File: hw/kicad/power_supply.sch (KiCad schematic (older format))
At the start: 30 parts, among them U10 LM22675-5.0, U8 LM22675-5.0, U9 AZ1117CR-3.3

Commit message: Changed footprint of and placed bulk cap
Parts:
- C52: footprint Capacitors_ThroughHole:C_Radial_D18_L36_P7.5 -> Capacitors_angled:C_Radial_D18_L37_P7.5_Angled
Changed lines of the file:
@@
 F 0 "C52" H 2275 2150 50  0000 L CNN
 F 1 "2200u/63V1" H 2275 1950 50  0000 L CNN
-F 2 "Capacitors_ThroughHole:C_Radial_D18_L36_P7.5" H 2288 1900 30  0001 C CNN
+F 2 "Capacitors_angled:C_Radial_D18_L37_P7.5_Angled" H 2288 1900 30  0001 C CNN
 F 3 "" H 2250 2050 60  0000 C CNN
 	1    2250 2050

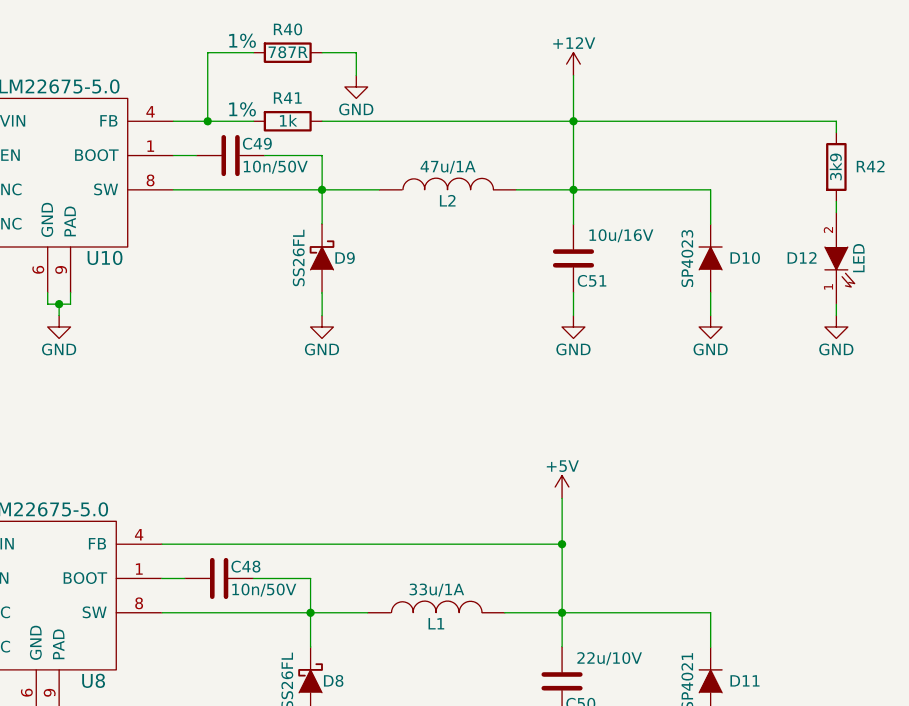
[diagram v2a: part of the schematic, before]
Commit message: Add test pads
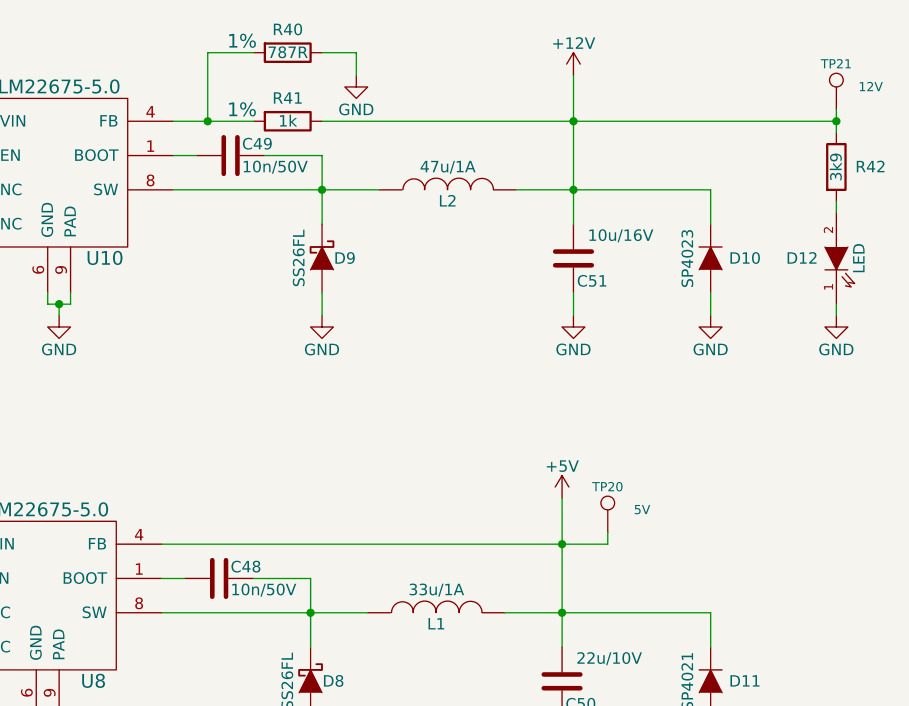
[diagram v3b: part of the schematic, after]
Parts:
- added TP20: 5V, Measurement_Points:Measurement_Point_Round-SMD-Pad_Small, symbol TESTPAD
- added TP21: 12V, Measurement_Points:Measurement_Point_Round-SMD-Pad_Small, symbol TESTPAD
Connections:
- net +12V: now also TP21.1
- net +5V: now also TP20.1
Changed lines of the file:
@@
 $EndDescr
 $Comp
-L +5V #PWR85
+L +5V #PWR077
 U 1 1 582A637E
 P 4500 5200
-F 0 "#PWR85" H 4500 5050 50  0001 C CNN
+F 0 "#PWR077" H 4500 5050 50  0001 C CNN
 F 1 "+5V" H 4500 5340 50  0000 C CNN
 F 2 "" H 4500 5200 60  0000 C CNN
@@
 $EndComp
 $Comp
-L +3.3V #PWR90
+L +3.3V #PWR078
 U 1 1 582A6384
 P 6050 5200
-F 0 "#PWR90" H 6050 5050 50  0001 C CNN
+F 0 "#PWR078" H 6050 5050 50  0001 C CNN
 F 1 "+3.3V" H 6050 5340 50  0000 C CNN
 F 2 "" H 6050 5200 60  0000 C CNN
@@
 Connection ~ 6050 5500
 $Comp
-L GND #PWR88
+L GND #PWR079
 U 1 1 582A63B6
 P 5400 6100
-F 0 "#PWR88" H 5400 5850 50  0001 C CNN
+F 0 "#PWR079" H 5400 5850 50  0001 C CNN
 F 1 "GND" H 5400 5950 50  0000 C CNN
 F 2 "" H 5400 6100 60  0000 C CNN
@@
 $EndComp
 $Comp
-L VPP #PWR77
+L VPP #PWR080
 U 1 1 582A6B17
 P 2250 1550
-F 0 "#PWR77" H 2250 1400 50  0001 C CNN
+F 0 "#PWR080" H 2250 1400 50  0001 C CNN
 F 1 "VPP" H 2250 1700 50  0000 C CNN
 F 2 "" H 2250 1550 60  0000 C CNN
@@
 $EndComp
 $Comp
-L GND #PWR78
+L GND #PWR081
 U 1 1 582A75C3
 P 2250 2600
-F 0 "#PWR78" H 2250 2350 50  0001 C CNN
+F 0 "#PWR081" H 2250 2350 50  0001 C CNN
 F 1 "GND" H 2250 2450 50  0000 C CNN
 F 2 "" H 2250 2600 60  0000 C CNN
@@
 	2250 1550 2250 1900
 $Comp
-L GND #PWR89
+L GND #PWR082
 U 1 1 5830BFE7
 P 5450 2600
-F 0 "#PWR89" H 5450 2350 50  0001 C CNN
+F 0 "#PWR082" H 5450 2350 50  0001 C CNN
 F 1 "GND" H 5450 2450 50  0000 C CNN
 F 2 "" H 5450 2600 60  0000 C CNN
@@
 	7700 1550 7700 2200
 $Comp
-L GND #PWR92
+L GND #PWR083
 U 1 1 5830D1D1
 P 6600 2600
-F 0 "#PWR92" H 6600 2350 50  0001 C CNN
+F 0 "#PWR083" H 6600 2350 50  0001 C CNN
 F 1 "GND" H 6600 2450 50  0000 C CNN
 F 2 "" H 6600 2600 60  0000 C CNN
@@
 	6600 2600 6600 2500
 $Comp
-L GND #PWR97
+L GND #PWR084
 U 1 1 5830D22E
 P 7700 2600
-F 0 "#PWR97" H 7700 2350 50  0001 C CNN
+F 0 "#PWR084" H 7700 2350 50  0001 C CNN
 F 1 "GND" H 7700 2450 50  0000 C CNN
 F 2 "" H 7700 2600 60  0000 C CNN
@@
 Connection ~ 7700 2050
 $Comp
-L GND #PWR93
+L GND #PWR085
 U 1 1 5830D3AE
 P 6750 1550
-F 0 "#PWR93" H 6750 1300 50  0001 C CNN
+F 0 "#PWR085" H 6750 1300 50  0001 C CNN
 F 1 "GND" H 6750 1400 50  0000 C CNN
 F 2 "" H 6750 1550 60  0000 C CNN
@@
 Connection ~ 3750 1750
 $Comp
-L GND #PWR83
+L GND #PWR086
 U 1 1 5830D719
 P 3750 2600
-F 0 "#PWR83" H 3750 2350 50  0001 C CNN
+F 0 "#PWR086" H 3750 2350 50  0001 C CNN
 F 1 "GND" H 3750 2450 50  0000 C CNN
 F 2 "" H 3750 2600 60  0000 C CNN
@@
 $EndComp
 $Comp
-L GND #PWR80
+L GND #PWR087
 U 1 1 5830D74E
 P 3350 2600
-F 0 "#PWR80" H 3350 2350 50  0001 C CNN
+F 0 "#PWR087" H 3350 2350 50  0001 C CNN
 F 1 "GND" H 3350 2450 50  0000 C CNN
 F 2 "" H 3350 2600 60  0000 C CNN
@@
 $EndComp
 $Comp
-L +12V #PWR96
+L +12V #PWR088
 U 1 1 5830E887
 P 7700 1550
-F 0 "#PWR96" H 7700 1400 50  0001 C CNN
+F 0 "#PWR088" H 7700 1400 50  0001 C CNN
 F 1 "+12V" H 7700 1690 50  0000 C CNN
 F 2 "" H 7700 1550 60  0000 C CNN
@@
 $EndComp
 $Comp
-L GND #PWR100
+L GND #PWR089
 U 1 1 5830FFA0
 P 8850 2600
-F 0 "#PWR100" H 8850 2350 50  0001 C CNN
+F 0 "#PWR089" H 8850 2350 50  0001 C CNN
 F 1 "GND" H 8850 2450 50  0000 C CNN
 F 2 "" H 8850 2600 60  0000 C CNN
@@
 $EndComp
 Wire Wire Line
-	8850 1750 8850 1800
+	8850 1700 8850 1800
 Wire Wire Line
 	8850 2150 8850 2100
 $Comp
-L GND #PWR87
+L GND #PWR090
 U 1 1 58310D16
 P 5400 4450
-F 0 "#PWR87" H 5400 4200 50  0001 C CNN
+F 0 "#PWR090" H 5400 4200 50  0001 C CNN
 F 1 "GND" H 5400 4300 50  0000 C CNN
 F 2 "" H 5400 4450 60  0000 C CNN
@@
 	7650 3400 7650 4050
 $Comp
-L GND #PWR91
+L GND #PWR091
 U 1 1 58310D5A
 P 6550 4450
-F 0 "#PWR91" H 6550 4200 50  0001 C CNN
+F 0 "#PWR091" H 6550 4200 50  0001 C CNN
 F 1 "GND" H 6550 4300 50  0000 C CNN
 F 2 "" H 6550 4450 60  0000 C CNN
@@
 	6550 4450 6550 4350
 $Comp
-L GND #PWR95
+L GND #PWR092
 U 1 1 58310D61
 P 7650 4450
-F 0 "#PWR95" H 7650 4200 50  0001 C CNN
+F 0 "#PWR092" H 7650 4200 50  0001 C CNN
 F 1 "GND" H 7650 4300 50  0000 C CNN
 F 2 "" H 7650 4450 60  0000 C CNN
@@
 Connection ~ 3750 3600
 $Comp
-L GND #PWR84
+L GND #PWR093
 U 1 1 58310D84
 P 3750 4450
-F 0 "#PWR84" H 3750 4200 50  0001 C CNN
+F 0 "#PWR093" H 3750 4200 50  0001 C CNN
 F 1 "GND" H 3750 4300 50  0000 C CNN
 F 2 "" H 3750 4450 60  0000 C CNN
@@
 $EndComp
 $Comp
-L GND #PWR82
+L GND #PWR094
 U 1 1 58310D8A
 P 3350 4450
-F 0 "#PWR82" H 3350 4200 50  0001 C CNN
+F 0 "#PWR094" H 3350 4200 50  0001 C CNN
 F 1 "GND" H 3350 4300 50  0000 C CNN
 F 2 "" H 3350 4450 60  0000 C CNN
@@
 Connection ~ 7650 3600
 $Comp
-L +5V #PWR94
+L +5V #PWR095
 U 1 1 583110A2
 P 7650 3400
-F 0 "#PWR94" H 7650 3250 50  0001 C CNN
+F 0 "#PWR095" H 7650 3250 50  0001 C CNN
 F 1 "+5V" H 7650 3540 50  0000 C CNN
 F 2 "" H 7650 3400 60  0000 C CNN
@@
 $EndComp
 Wire Wire Line
-	5900 3600 7650 3600
+	5900 3600 7850 3600
 $Comp
 L D_Schottky D9
@@
 $EndComp
 $Comp
-L VPP #PWR79
+L VPP #PWR096
 U 1 1 583126D7
 P 3350 1550
-F 0 "#PWR79" H 3350 1400 50  0001 C CNN
+F 0 "#PWR096" H 3350 1400 50  0001 C CNN
 F 1 "VPP" H 3350 1700 50  0000 C CNN
 F 2 "" H 3350 1550 60  0000 C CNN
@@
 Connection ~ 3350 1750
 $Comp
-L VPP #PWR81
+L VPP #PWR097
 U 1 1 583129B0
 P 3350 3400
-F 0 "#PWR81" H 3350 3250 50  0001 C CNN
+F 0 "#PWR097" H 3350 3250 50  0001 C CNN
 F 1 "VPP" H 3350 3550 50  0000 C CNN
 F 2 "" H 3350 3400 60  0000 C CNN
@@
 Connection ~ 4800 1900
 $Comp
-L GND #PWR86
+L GND #PWR098
 U 1 1 58336406
 P 4800 2600
-F 0 "#PWR86" H 4800 2350 50  0001 C CNN
+F 0 "#PWR098" H 4800 2350 50  0001 C CNN
 F 1 "GND" H 4800 2450 50  0000 C CNN
 F 2 "" H 4800 2600 60  0000 C CNN
@@
 	8300 2050 8300 2200
 $Comp
-L GND #PWR98
+L GND #PWR099
 U 1 1 583A15DE
 P 8300 2600
-F 0 "#PWR98" H 8300 2350 50  0001 C CNN
+F 0 "#PWR099" H 8300 2350 50  0001 C CNN
 F 1 "GND" H 8300 2450 50  0000 C CNN
 F 2 "" H 8300 2600 60  0000 C CNN
@@
 	8300 3900 8300 4050
 $Comp
-L GND #PWR99
+L GND #PWR0100
 U 1 1 583A21F7
 P 8300 4450
-F 0 "#PWR99" H 8300 4200 50  0001 C CNN
+F 0 "#PWR0100" H 8300 4200 50  0001 C CNN
 F 1 "GND" H 8300 4300 50  0000 C CNN
 F 2 "" H 8300 4450 60  0000 C CNN
@@
 	0    1    1    0
 $EndComp
+$Comp
+L TESTPAD TP21
+U 1 1 5856EA7E
+P 8850 1650
+F 0 "TP21" H 8850 1800 40  0000 C CNN
+F 1 "12V" H 9000 1700 40  0000 C CNN
+F 2 "Measurement_Points:Measurement_Point_Round-SMD-Pad_Small" V 8850 1800 60  0001 C CNN
+F 3 "" V 8850 1800 60  0000 C CNN
+	1    8850 1650
+	1    0    0    -1
+$EndComp
+Connection ~ 8850 1750
+$Comp
+L TESTPAD TP20
+U 1 1 5856EC9B
+P 7850 3500
+F 0 "TP20" H 7850 3650 40  0000 C CNN
+F 1 "5V" H 8000 3550 40  0000 C CNN
+F 2 "Measurement_Points:Measurement_Point_Round-SMD-Pad_Small" V 7850 3650 60  0001 C CNN
+F 3 "" V 7850 3650 60  0000 C CNN
+	1    7850 3500
+	1    0    0    -1
+$EndComp
+Wire Wire Line
+	7850 3600 7850 3550
 $EndSCHEMATC
